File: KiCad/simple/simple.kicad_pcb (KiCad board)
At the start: 2 copper layers, 26.4 x 13.7 mm, 11 parts, among them IC1 PIC16F15213T-I_SN, J1 Conn_01x02, J2 Conn_01x02, J3 Conn_01x01, J5 Conn_01x02

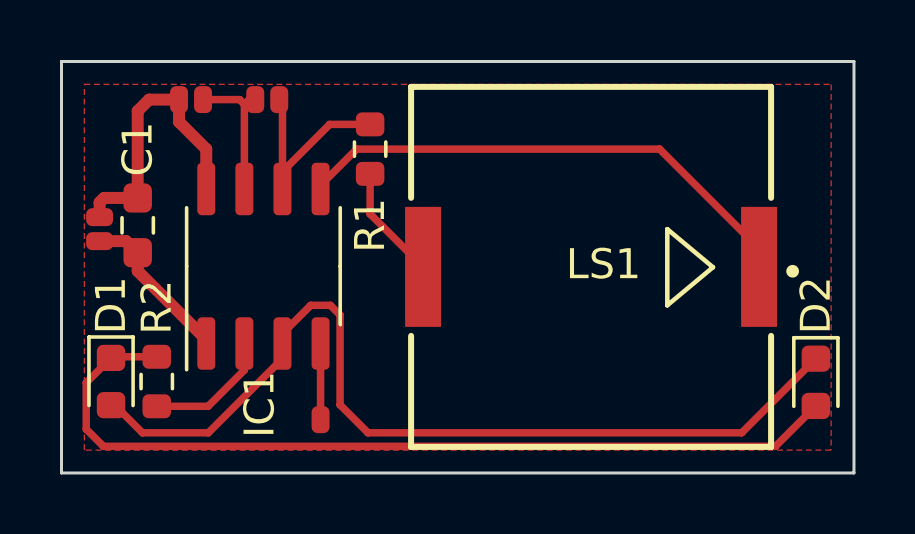
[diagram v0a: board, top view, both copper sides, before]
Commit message: Fix the footprint of C1
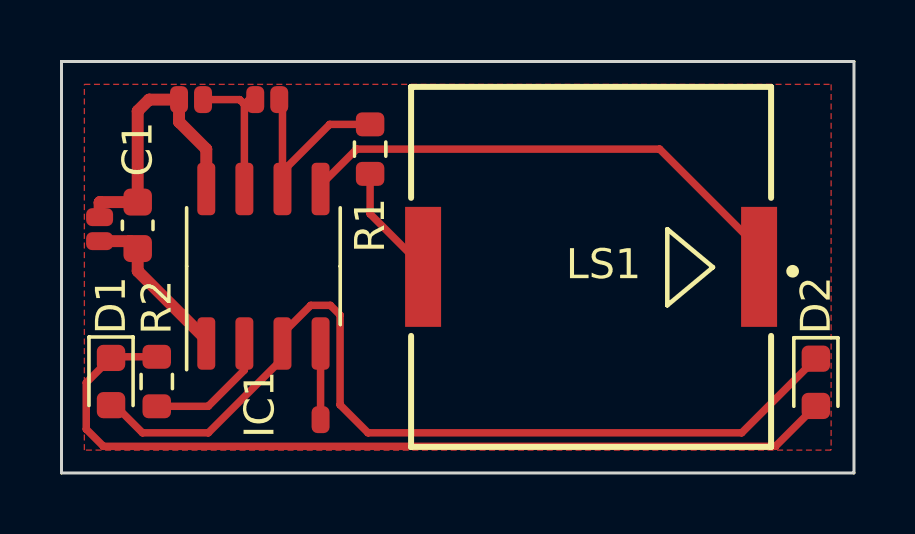
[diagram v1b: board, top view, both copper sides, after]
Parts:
- C1: footprint Resistor_SMD:R_0603_1608Metric_Pad0.98x0.95mm_HandSolder -> Capacitor_SMD:C_0603_1608Metric
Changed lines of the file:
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@@
   (title_block
     (title "Wazuka-Crossing - Simple Version")
-    (date "2023-07-31")
-    (rev "0")
+    (date "2023-08-17")
+    (rev "1")
     (company "Wazuka Chagenkyo Railway")
   )
@@
     )
     (pad_to_mask_clearance 0)
+    (aux_axis_origin 62.992 64.008)
     (pcbplotparams
       (layerselection 0x00010fc_ffffffff)
@@
       (net 10 "Net-(LS1--)") (pinfunction "-") (pintype "passive"))
   )
-  (footprint "Resistor_SMD:R_0603_1608Metric_Pad0.98x0.95mm_HandSolder" (layer "F.Cu")
+  (footprint "Capacitor_SMD:C_0603_1608Metric" (layer "F.Cu")
     (at 65.532 55.753 90)
-    (descr "Resistor SMD 0603 (1608 Metric), square (rectangular) end terminal, IPC_7351 nominal with elongated pad for handsoldering. (Body size source: IPC-SM-782 page 72, https://www.pcb-3d.com/wordpress/wp-content/uploads/ipc-sm-782a_amendment_1_and_2.pdf), generated with kicad-footprint-generator")
-    (tags "resistor handsolder")
+    (descr "Capacitor SMD 0603 (1608 Metric), square (rectangular) end terminal, IPC_7351 nominal, (Body size source: IPC-SM-782 page 76, https://www.pcb-3d.com/wordpress/wp-content/uploads/ipc-sm-782a_amendment_1_and_2.pdf), generated with kicad-footprint-generator")
+    (tags "capacitor")
     (property "Sheetfile" "simple.kicad_sch")
     (property "Sheetname" "")
@@
         (effects (font (size 1 1) (thickness 0.15)))
     )
-    (fp_text value "0.1u" (at 0.508 1.143 90) (layer "F.Fab")
+    (fp_text value "0.1u" (at 0 1.43 90) (layer "F.Fab")
         (effects (font (size 1 1) (thickness 0.15)))
     )
@@
         (effects (font (size 0.4 0.4) (thickness 0.06)))
     )
-    (fp_line (start -0.254724 -0.5225) (end 0.254724 -0.5225)
-      (stroke (width 0.12) (type solid)) (layer "F.SilkS"))
-    (fp_line (start -0.254724 0.5225) (end 0.254724 0.5225)
-      (stroke (width 0.12) (type solid)) (layer "F.SilkS"))
-    (fp_line (start -1.65 -0.73) (end 1.65 -0.73)
-      (stroke (width 0.05) (type solid)) (layer "F.CrtYd"))
-    (fp_line (start -1.65 0.73) (end -1.65 -0.73)
-      (stroke (width 0.05) (type solid)) (layer "F.CrtYd"))
-    (fp_line (start 1.65 -0.73) (end 1.65 0.73)
-      (stroke (width 0.05) (type solid)) (layer "F.CrtYd"))
-    (fp_line (start 1.65 0.73) (end -1.65 0.73)
-      (stroke (width 0.05) (type solid)) (layer "F.CrtYd"))
-    (fp_line (start -0.8 -0.4125) (end 0.8 -0.4125)
-      (stroke (width 0.1) (type solid)) (layer "F.Fab"))
-    (fp_line (start -0.8 0.4125) (end -0.8 -0.4125)
-      (stroke (width 0.1) (type solid)) (layer "F.Fab"))
-    (fp_line (start 0.8 -0.4125) (end 0.8 0.4125)
-      (stroke (width 0.1) (type solid)) (layer "F.Fab"))
-    (fp_line (start 0.8 0.4125) (end -0.8 0.4125)
-      (stroke (width 0.1) (type solid)) (layer "F.Fab"))
-    (pad "1" smd roundrect (at -0.9125 0 90) (size 0.975 0.95) (layers "F.Cu" "F.Paste" "F.Mask") (roundrect_rratio 0.25)
+    (fp_line (start -0.14058 -0.51) (end 0.14058 -0.51)
+      (stroke (width 0.12) (type solid)) (layer "F.SilkS"))
+    (fp_line (start -0.14058 0.51) (end 0.14058 0.51)
+      (stroke (width 0.12) (type solid)) (layer "F.SilkS"))
+    (fp_line (start -1.48 -0.73) (end 1.48 -0.73)
+      (stroke (width 0.05) (type solid)) (layer "F.CrtYd"))
+    (fp_line (start -1.48 0.73) (end -1.48 -0.73)
+      (stroke (width 0.05) (type solid)) (layer "F.CrtYd"))
+    (fp_line (start 1.48 -0.73) (end 1.48 0.73)
+      (stroke (width 0.05) (type solid)) (layer "F.CrtYd"))
+    (fp_line (start 1.48 0.73) (end -1.48 0.73)
+      (stroke (width 0.05) (type solid)) (layer "F.CrtYd"))
+    (fp_line (start -0.8 -0.4) (end 0.8 -0.4)
+      (stroke (width 0.1) (type solid)) (layer "F.Fab"))
+    (fp_line (start -0.8 0.4) (end -0.8 -0.4)
+      (stroke (width 0.1) (type solid)) (layer "F.Fab"))
+    (fp_line (start 0.8 -0.4) (end 0.8 0.4)
+      (stroke (width 0.1) (type solid)) (layer "F.Fab"))
+    (fp_line (start 0.8 0.4) (end -0.8 0.4)
+      (stroke (width 0.1) (type solid)) (layer "F.Fab"))
+    (pad "1" smd roundrect (at -0.775 0 90) (size 0.9 0.95) (layers "F.Cu" "F.Paste" "F.Mask") (roundrect_rratio 0.25)
       (net 1 "+BATT") (pintype "passive"))
-    (pad "2" smd roundrect (at 0.9125 0 90) (size 0.975 0.95) (layers "F.Cu" "F.Paste" "F.Mask") (roundrect_rratio 0.25)
+    (pad "2" smd roundrect (at 0.775 0 90) (size 0.9 0.95) (layers "F.Cu" "F.Paste" "F.Mask") (roundrect_rratio 0.25)
       (net 2 "GND") (pintype "passive"))
-    (model "${KICAD6_3DMODEL_DIR}/Resistor_SMD.3dshapes/R_0603_1608Metric.wrl"
+    (model "${KICAD6_3DMODEL_DIR}/Capacitor_SMD.3dshapes/C_0603_1608Metric.wrl"
       (offset (xyz 0 0 0))
       (scale (xyz 1 1 1))
@@
     (style (thickness 0.15) (arrow_length 1.27) (text_position_mode 0) (extension_height 0.58642) (extension_offset 0.5) keep_text_aligned)
   )
-  (segment (start 65.532 56.6655) (end 65.532 57.277) (width 0.4) (layer "F.Cu") (net 1))
   (segment (start 65.532 57.277) (end 67.818 59.563) (width 0.4) (layer "F.Cu") (net 1))
+  (segment (start 65.532 56.528) (end 65.532 57.277) (width 0.4) (layer "F.Cu") (net 1))
+  (segment (start 65.284 56.28) (end 65.532 56.528) (width 0.4) (layer "F.Cu") (net 1))
+  (segment (start 64.262 56.28) (end 65.284 56.28) (width 0.4) (layer "F.Cu") (net 1))
   (segment (start 67.818 59.563) (end 67.818 59.817) (width 0.4) (layer "F.Cu") (net 1))
-  (segment (start 64.262 56.28) (end 65.1465 56.28) (width 0.4) (layer "F.Cu") (net 1))
-  (segment (start 65.1465 56.28) (end 65.532 56.6655) (width 0.4) (layer "F.Cu") (net 1))
-  (segment (start 64.4125 54.8405) (end 65.405 54.8405) (width 0.4) (layer "F.Cu") (net 2))
-  (segment (start 64.262 55.48) (end 64.262 54.991) (width 0.4) (layer "F.Cu") (net 2))
-  (segment (start 65.532 51.943) (end 65.913 51.562) (width 0.4) (layer "F.Cu") (net 2))
-  (segment (start 65.532 54.8405) (end 65.532 51.943) (width 0.4) (layer "F.Cu") (net 2))
+  (segment (start 64.262 54.991) (end 64.275 54.978) (width 0.4) (layer "F.Cu") (net 2))
   (segment (start 65.913 51.562) (end 66.91 51.562) (width 0.4) (layer "F.Cu") (net 2))
-  (segment (start 64.262 54.991) (end 64.4125 54.8405) (width 0.4) (layer "F.Cu") (net 2))
+  (segment (start 65.532 54.978) (end 65.532 51.943) (width 0.4) (layer "F.Cu") (net 2))
+  (segment (start 64.275 54.978) (end 65.532 54.978) (width 0.4) (layer "F.Cu") (net 2))
   (segment (start 67.818 54.417) (end 67.818 53.213) (width 0.4) (layer "F.Cu") (net 2))
   (segment (start 66.91 52.305) (end 66.91 51.562) (width 0.4) (layer "F.Cu") (net 2))
+  (segment (start 65.532 51.943) (end 65.913 51.562) (width 0.4) (layer "F.Cu") (net 2))
+  (segment (start 64.262 55.48) (end 64.262 54.991) (width 0.4) (layer "F.Cu") (net 2))
   (segment (start 67.818 53.213) (end 66.91 52.305) (width 0.4) (layer "F.Cu") (net 2))
   (segment (start 63.817 60.9985) (end 63.817 62.547) (width 0.25) (layer "F.Cu") (net 3))
